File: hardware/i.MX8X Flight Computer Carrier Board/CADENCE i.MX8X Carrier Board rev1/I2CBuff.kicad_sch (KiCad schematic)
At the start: 23 parts, among them U20 P82B715DR, U21 P82B715DR, U22 P82B715DR

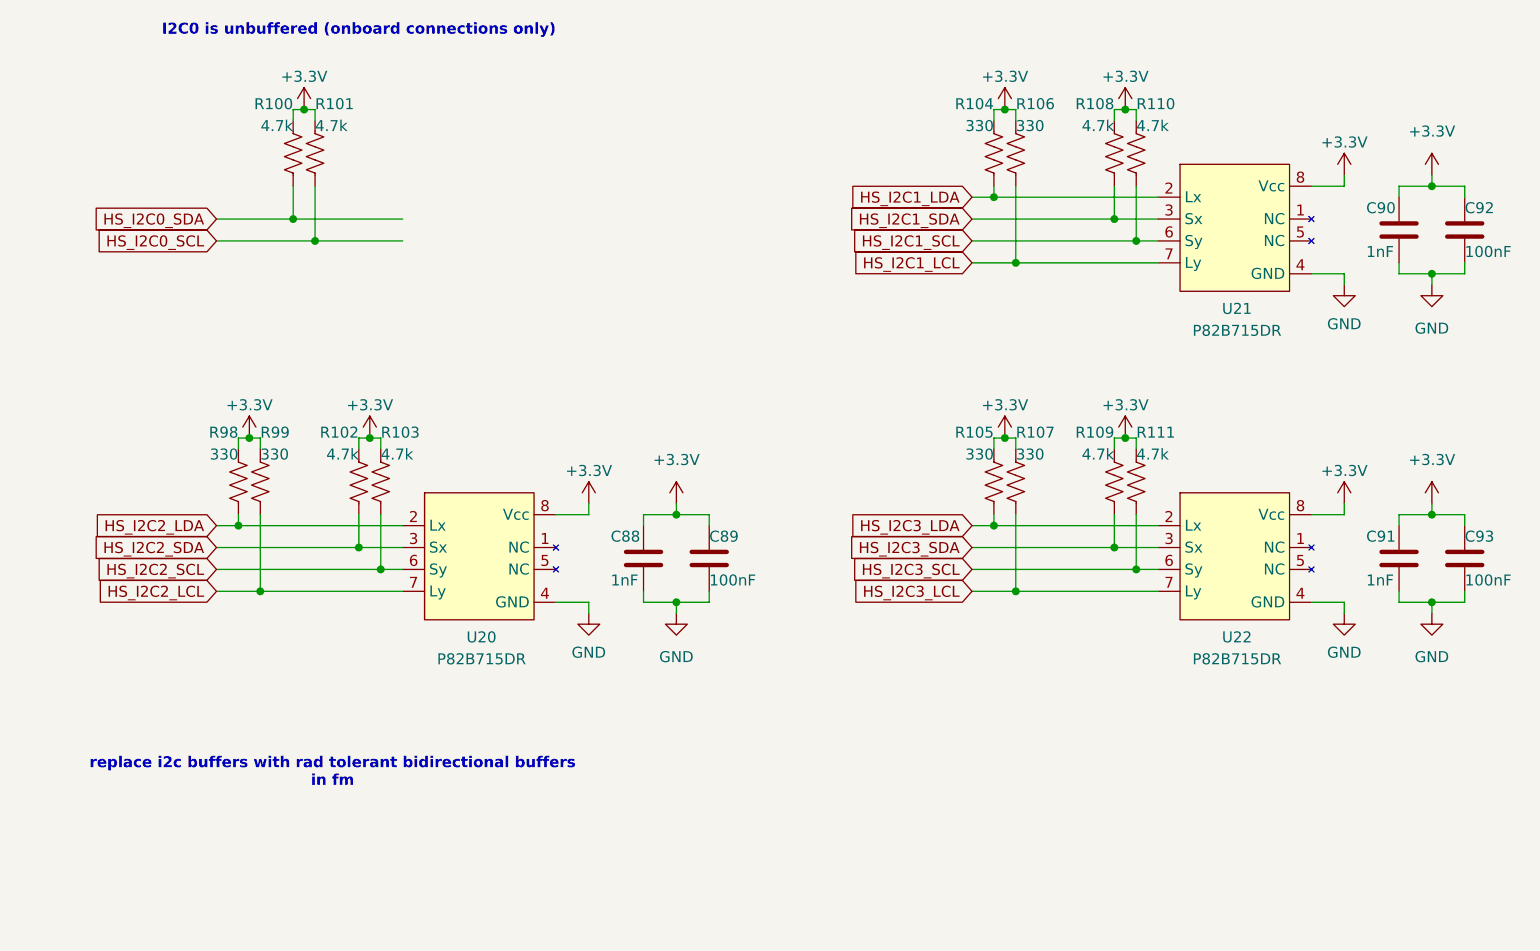
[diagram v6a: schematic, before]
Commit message: cchanges after phytec review
- fixed issue with ospi chip select line & clk line
- replaced 1k pulldowns with 10k pulldowns and added 1k series resistors to 1.8V line for boot config lines
-removed unused global label tags from som and changed to nc
- repinmuxed for potential watchdog and ospi changes

to do:
-microSD
-reallocate gpios (extras to breakout)
-create 8pin jst connector for lucid camera (12V pwr)
- give satnogs additional uart
- reorg/rename global labels
-watchdog input pin reassign to c62 potentially after feedback from max
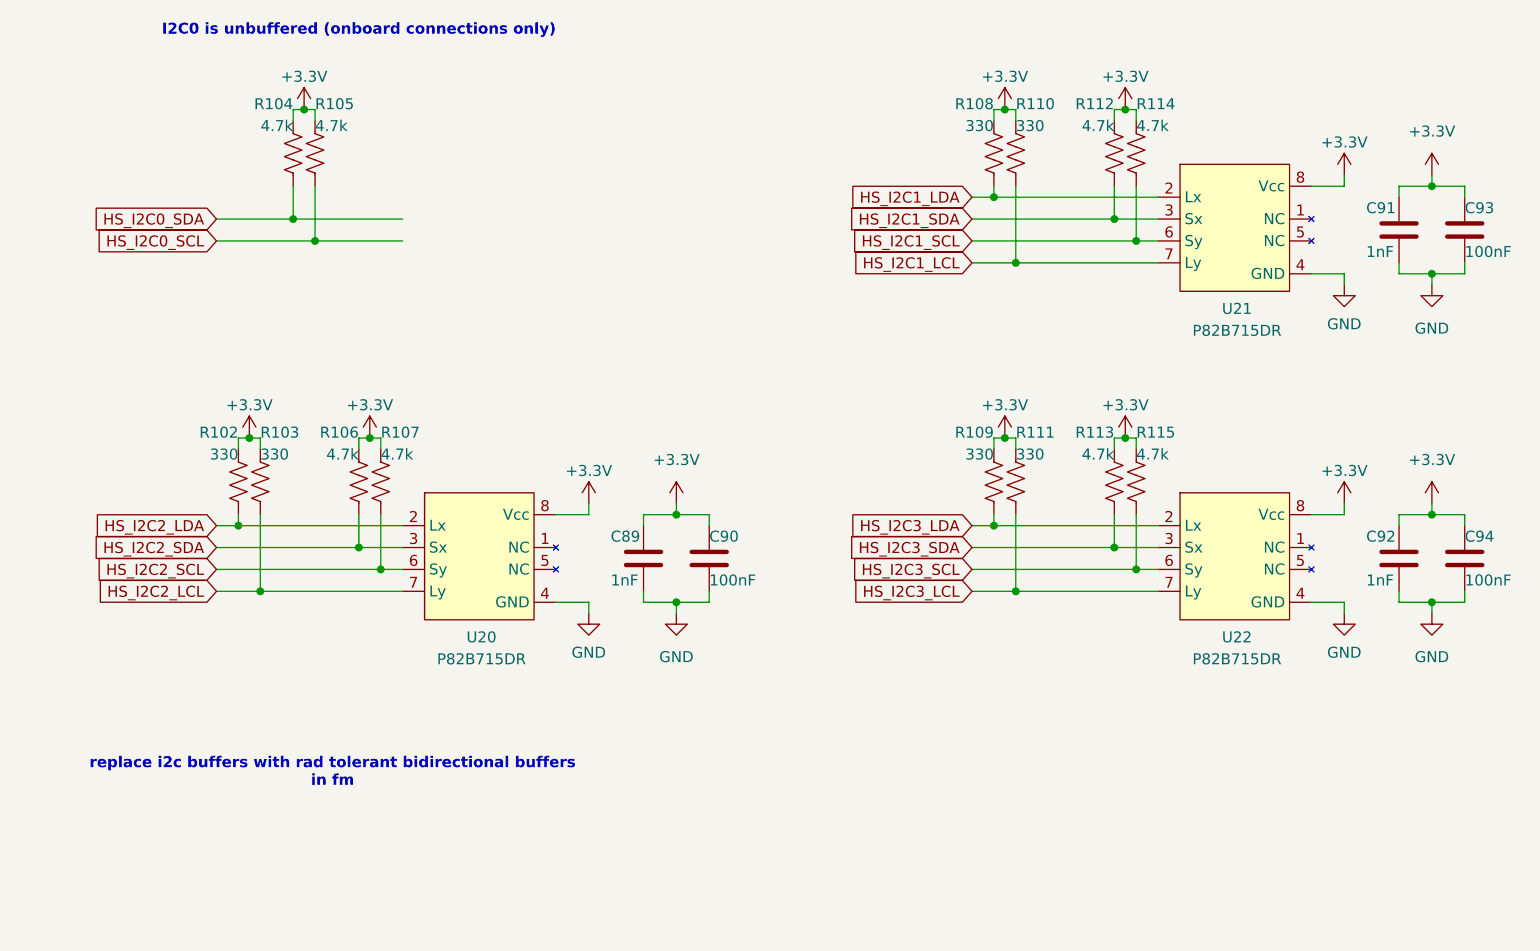
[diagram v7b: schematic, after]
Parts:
- renumbered C88 to C89, C89 to C90, C90 to C91, C91 to C92, C92 to C93, C93 to C94, R98 to R102, R99 to R103, R100 to R104, R101 to R105, R102 to R106, R103 to R107, R104 to R108, R105 to R109, R106 to R110, R107 to R111, R108 to R112, R109 to R113, R110 to R114, R111 to R115

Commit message: Finished footprints- Double check usbs
Only thing i didn't touch was watchdogs. That might still need to be changed.
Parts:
- C89, C90, C91, C92, C93, C94: footprint Capacitor_SMD:C_0603_1608Metric -> Capacitor_SMD:C_0402_1005Metric
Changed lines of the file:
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@@
 			)
 		)
-		(property "Footprint" "Capacitor_SMD:C_0603_1608Metric"
+		(property "Footprint" "Capacitor_SMD:C_0402_1005Metric"
 			(at 185.1152 49.53 0)
 			(effects
@@
 			)
 		)
-		(property "Footprint" "Capacitor_SMD:C_0603_1608Metric"
+		(property "Footprint" "Capacitor_SMD:C_0402_1005Metric"
 			(at 185.1152 87.63 0)
 			(effects
@@
 			)
 		)
-		(property "Footprint" "Capacitor_SMD:C_0603_1608Metric"
+		(property "Footprint" "Capacitor_SMD:C_0402_1005Metric"
 			(at 97.4852 87.63 0)
 			(effects
@@
 			)
 		)
-		(property "Footprint" "Capacitor_SMD:C_0603_1608Metric"
+		(property "Footprint" "Capacitor_SMD:C_0402_1005Metric"
 			(at 177.4952 87.63 0)
 			(effects
@@
 			)
 		)
-		(property "Footprint" "Capacitor_SMD:C_0603_1608Metric"
+		(property "Footprint" "Capacitor_SMD:C_0402_1005Metric"
 			(at 89.8652 87.63 0)
 			(effects
@@
 			)
 		)
-		(property "Footprint" "Capacitor_SMD:C_0603_1608Metric"
+		(property "Footprint" "Capacitor_SMD:C_0402_1005Metric"
 			(at 177.4952 49.53 0)
 			(effects
